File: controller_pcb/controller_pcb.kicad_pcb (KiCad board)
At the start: 2 copper layers, 64.5 x 53.5 mm, 26 parts, among them IC1 AMS1117-5.0, J1 A_08-LC-TT, J2 SM03B-GHS-TB_LF__SN_, Q1 SI2301CDS-T1-GE3.

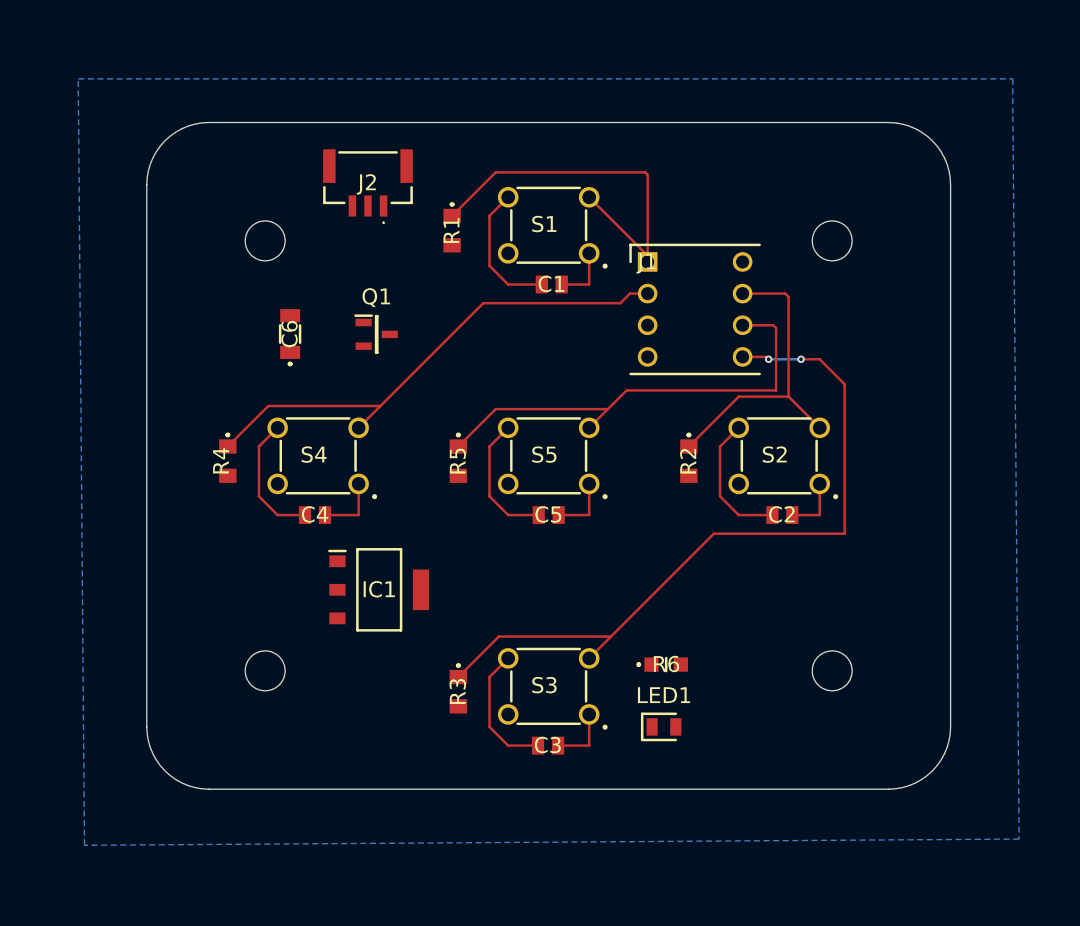
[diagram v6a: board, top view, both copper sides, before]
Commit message: Finished routing; added copper plane on front
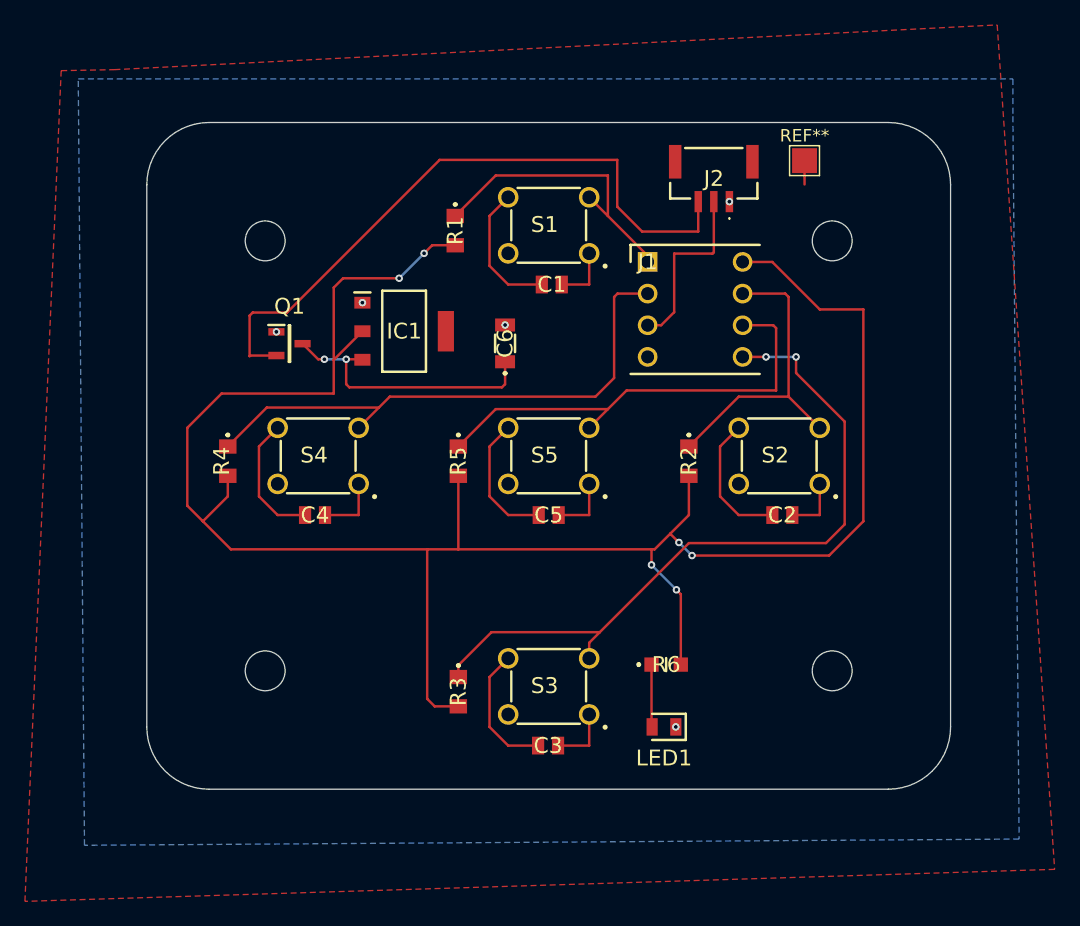
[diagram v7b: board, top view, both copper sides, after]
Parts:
- added REF**: TestPoint_Pad_2.0x2.0mm, TestPoint:TestPoint_Pad_2.0x2.0mm, F.Cu at (153.8, 103.6)
- moved J2 27.8 mm to (146.5, 105.0)
- moved IC1 20.8 mm to (121.7, 117.2)
- moved C6 17.3 mm to (129.8, 118.2)
- moved Q1 7.04 mm to (112.5, 118.2)
- moved R1 0.25 mm to (125.8, 109.2)
- turned LED1 to 180 degrees
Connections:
- J1 pad 3: unconnected-(J1-Pad3) -> Net-(J1-Pad3)
- J1 pad 5: Net-(IC1-VOUT) -> Net-(J1-Pad5)
- J2 pad 2: unconnected-(J2-Pad2) -> Net-(J1-Pad3)
- R3 pad 1: Net-(IC1-VOUT) -> Net-(J1-Pad5)
- R5 pad 1: Net-(IC1-VOUT) -> Net-(J1-Pad6)
- R5 pad 2: Net-(J1-Pad6) -> Net-(IC1-VOUT)
- S2 pad 3: Net-(IC1-VOUT) -> Net-(J1-Pad7)
- S3 pad 3: Net-(IC1-VOUT) -> Net-(J1-Pad5)
- S5 pad 3: Net-(IC1-VOUT) -> Net-(J1-Pad6)
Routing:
- net Net-(IC1-VOUT): track 96.6 -> 169.2 mm, vias 2 -> 6
- net Net-(J1-Pad5): track 0.00 -> 58.6 mm, vias 0 -> 2
- net Net-(Q1-S): track 0.00 -> 53.6 mm
- net Net-(J1-Pad6): track 0.00 -> 37.3 mm
- net Net-(IC1-VIN): track 0.00 -> 22.1 mm, vias 0 -> 2
- net Net-(J1-Pad3): track 0.00 -> 14.6 mm
- net Net-(J1-Pad1): track 31.4 -> 24.0 mm
- net Net-(LED1-A): track 0.00 -> 5.02 mm
- net Net-(J1-Pad2): track 41.2 -> 44.9 mm
- net (no net): track 0.00 -> 1.91 mm
- net GND: vias 0 -> 5
- added copper zone on F.Cu, net (none)

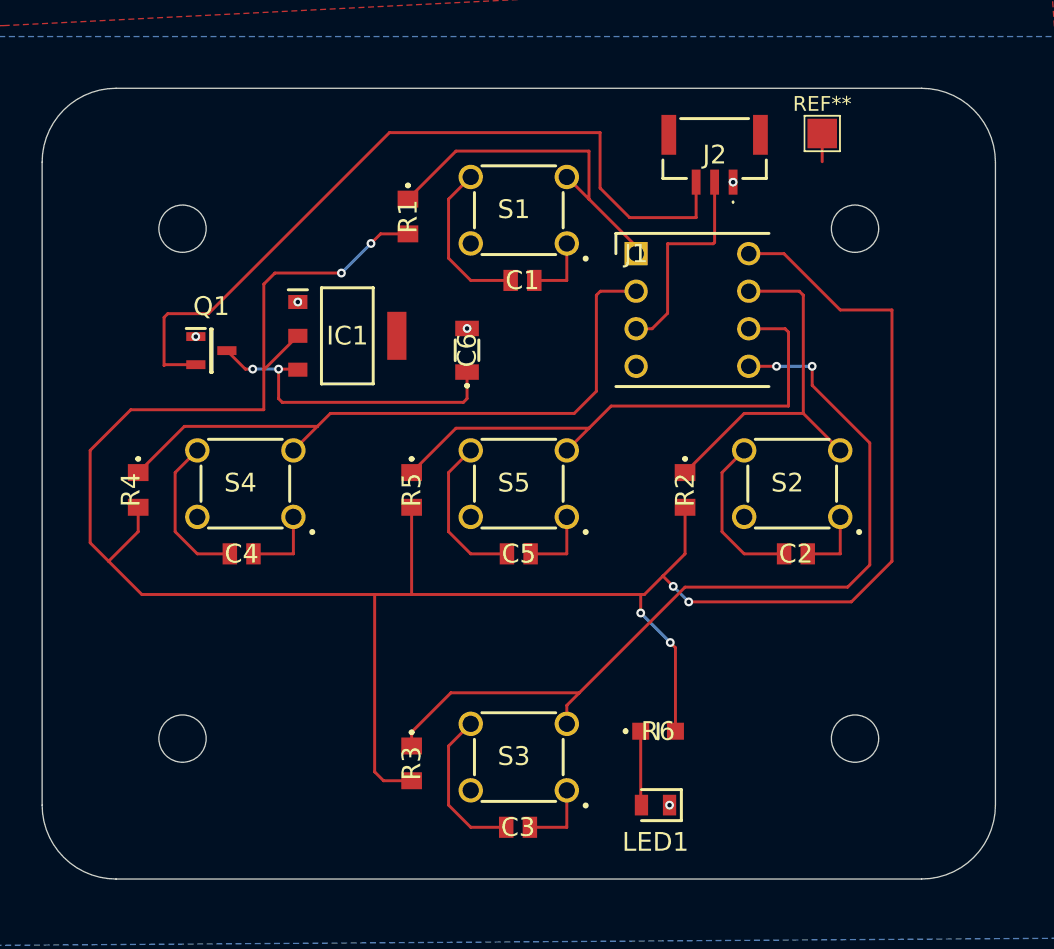
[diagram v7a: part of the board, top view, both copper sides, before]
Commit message: Rerouted for button clearance
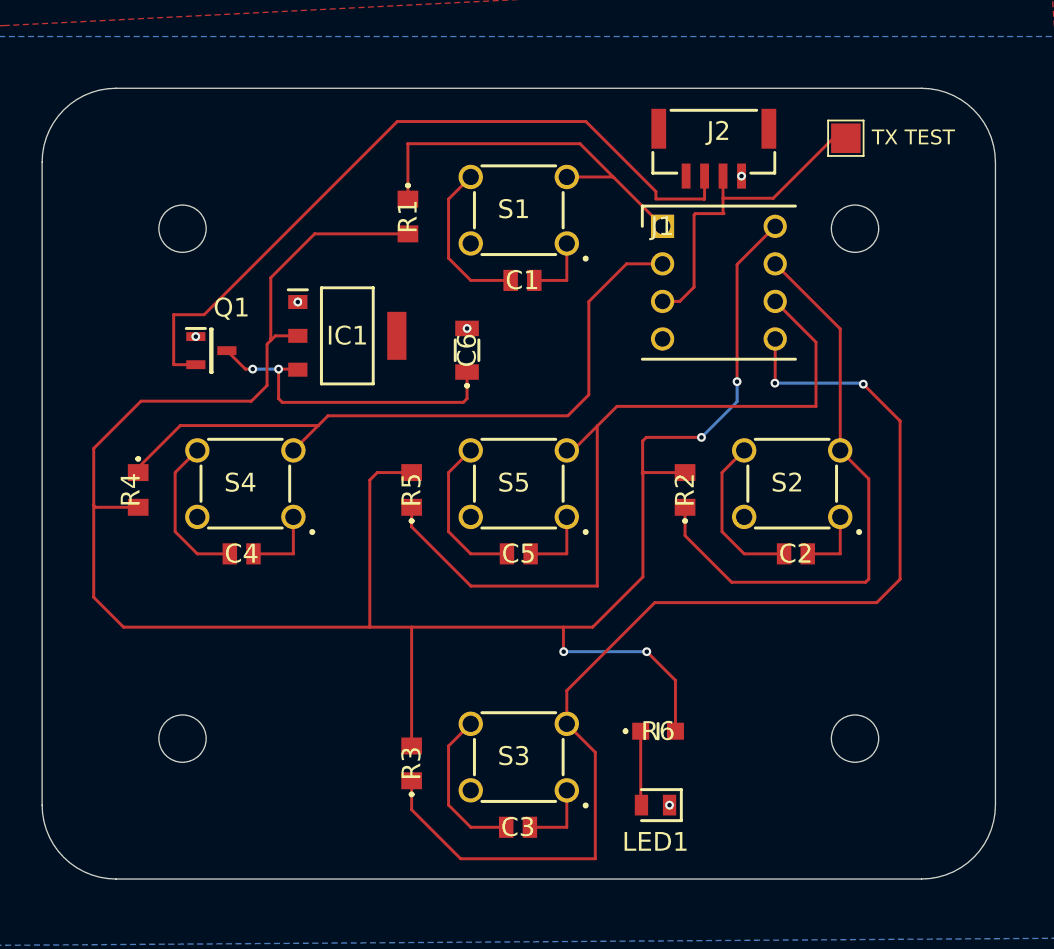
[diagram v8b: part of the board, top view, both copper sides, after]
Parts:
- removed the REF** at (153.8, 103.6)
- added TX TEST: TestPoint, TestPoint:TestPoint_Pad_2.0x2.0mm, F.Cu at (155.4, 103.9)
- J2: value SM03B-GHS-TB_LF__SN_ -> SM04B-GHS-TB_LF__SN_; footprint Controller_Footprints:SM03BGHSTBLFSN -> Controller_Footprints:SM04B-GHS-TB
- moved J1 2.57 mm to (143.0, 109.8)
- moved J2 1.24 mm to (146.4, 106.2)
- turned R2 to 90 degrees
- turned R3 to 90 degrees
- turned R5 to 90 degrees
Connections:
- J2 pad 5: unconnected-(J2-MP_2-Pad5) -> (no net)
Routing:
- net Net-(J1-Pad5): track 58.6 -> 76.9 mm
- net Net-(IC1-VOUT): track 169.2 -> 152.9 mm, vias 6 -> 4
- net Net-(J1-Pad6): track 37.3 -> 52.7 mm
- net Net-(J1-Pad7): track 25.0 -> 39.7 mm
- net Net-(J1-Pad3): track 14.6 -> 22.0 mm
- net Net-(Q1-S): track 53.6 -> 50.2 mm
- net Net-(J1-Pad2): track 44.9 -> 47.6 mm
- net Net-(J1-Pad1): track 24.0 -> 26.5 mm
- net (no net): track 1.91 -> 0.00 mm
